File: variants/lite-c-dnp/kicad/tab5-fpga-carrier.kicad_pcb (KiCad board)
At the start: 4 copper layers, 125 x 78 mm, 116 parts, among them J1 DC 12V ONLY, J2 USB-C PD in, J3 M5-BUS (to Tab5), J4 SOCKET XDAP-4042044-20401, J5 HDMI OUT, J6 PMOD1, J7 PMOD2, J8 GPIO pads, Q1 2N7002, Q2 2N7002, Q3 2N7002, Q4 2N7002, SW1 SW, SW2 RESET (Tab5), SW3 FPGA ON/OFF, U1 CH224K, U10 TPS3839K50DBZR, U2 TPS5430DDAR, U3 XC6206P332MR-G, U4 RCLAMP0524P, U5 RCLAMP0524P, U6 SRV05-4, U7 SN74CB3Q3245PWR, U8 SN74CB3Q3245PWR, U9 TPS3839G33DBZR

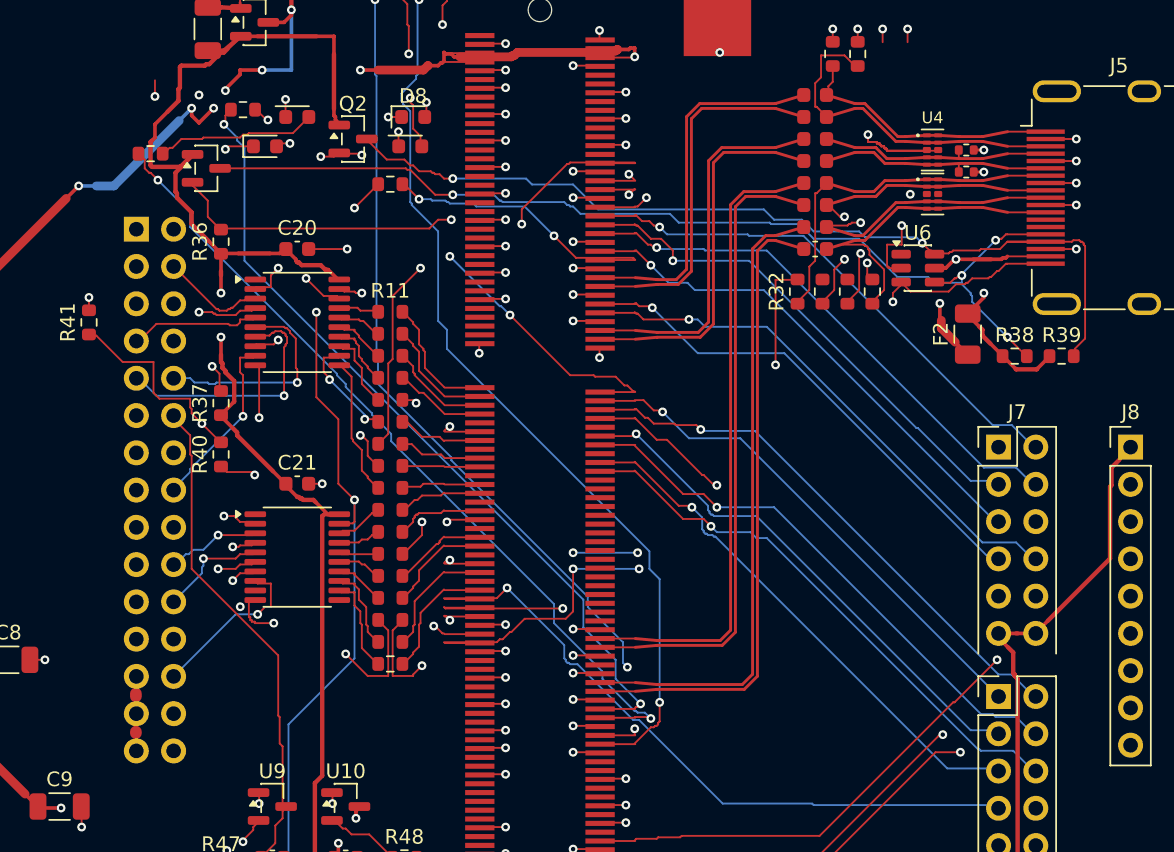
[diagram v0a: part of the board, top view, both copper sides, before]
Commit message: Qualify lite variants for conditional PoC fabrication and publish per-board reports
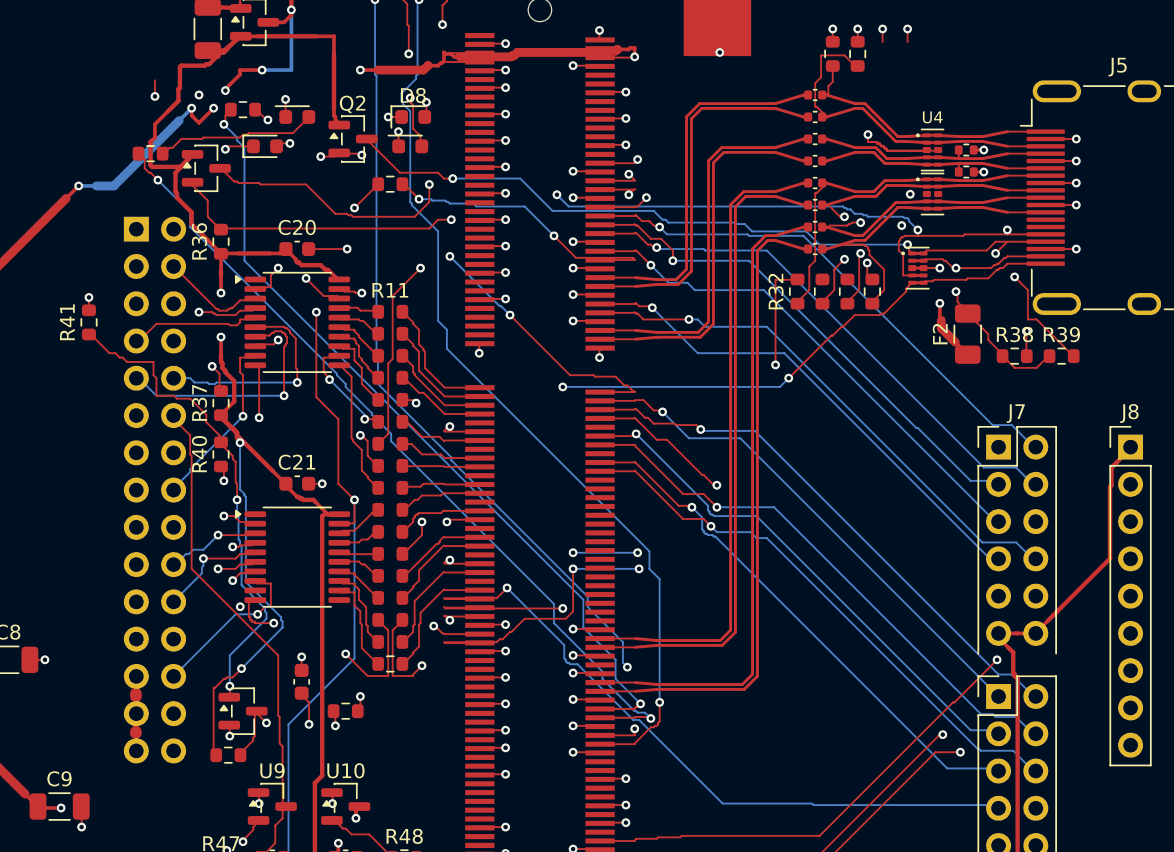
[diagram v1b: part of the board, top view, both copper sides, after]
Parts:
- added C24: 100n, C_0603_1608Metric, F.Cu at (65.0, 53.0)
- added Q5: MMBT3904, SOT-23, F.Cu at (61.0, 55.0)
- added R51: 47k, R_0603_1608Metric, F.Cu at (60.0, 58.0)
- added R52: 10k, R_0603_1608Metric, F.Cu at (68.0, 55.0)
- C12, C13, C14, C15, C16, C17, C18, C19: footprint C_0603_1608Metric -> C_0402_1005Metric
- R10, R11, R12, R13, R14, R15, R16, R19, R20, R21, R22, R23, R24, R26, R27: value 33R -> 680R
- R40: value 10k -> 47k
- R41: value 20k -> 100k
- U6: value SRV05-4 -> RCLAMP0524P; footprint SOT-23-6 -> DFN2510-10L_RCLAMP0524P
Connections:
- R40 pad 2: F_HPD -> HPD_B
- R41 pad 1: F_HPD -> HPD_B
- U6 pad 1: (no net) -> HDMI_SDA
- U6 pad 2: GND -> HDMI_5V
- U6 pad 3: HDMI_HPD -> GND
- U6 pad 5: HDMI_5V -> HDMI_HPD
- U6 pad 6: HDMI_SDA -> HDMI_HPD
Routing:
- net HPD_B: track 0.00 -> 33.4 mm, vias 0 -> 2
- net +3V3: track 189.1 -> 216.4 mm, vias 3 -> 5
- net HPD_BUF: track 0.00 -> 12.7 mm, vias 0 -> 3
- net HDMI_SCL: track 70.2 -> 76.8 mm, vias 4 -> 5
- net F_HPD: track 54.0 -> 48.2 mm
- net HDMI_SDA: track 63.3 -> 61.5 mm, vias 2 -> 4
- net HDMI_5V: track 20.9 -> 21.7 mm
- net HDMI_HPD: track 63.3 -> 64.1 mm, vias 2 -> 3
- net GND: track 187.6 -> 188.1 mm, vias 109 -> 112

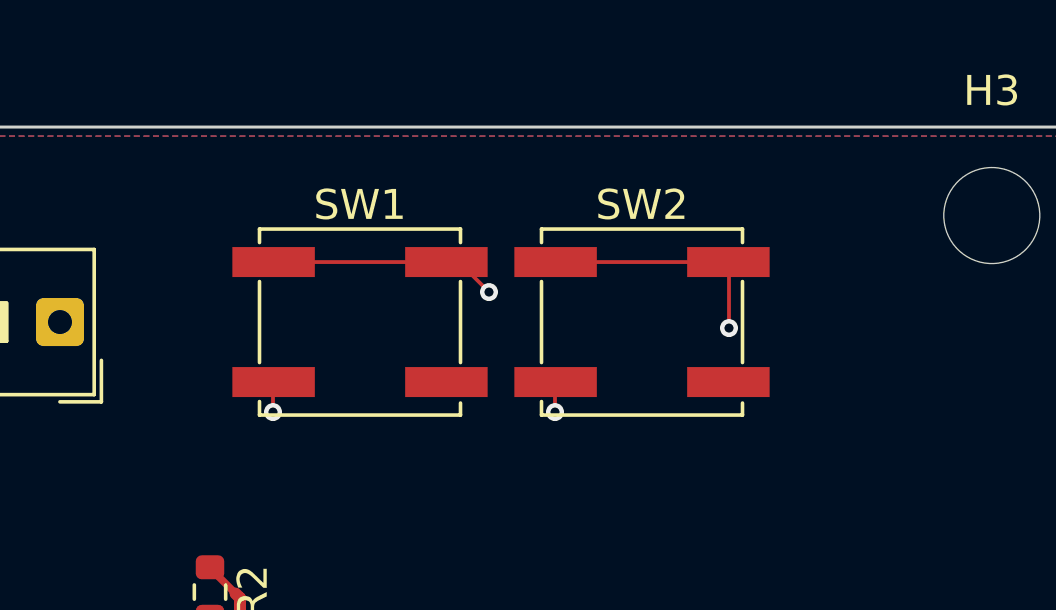
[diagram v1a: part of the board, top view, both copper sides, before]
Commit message: Align variants B and C with Akizuki buttons and explain A BOM
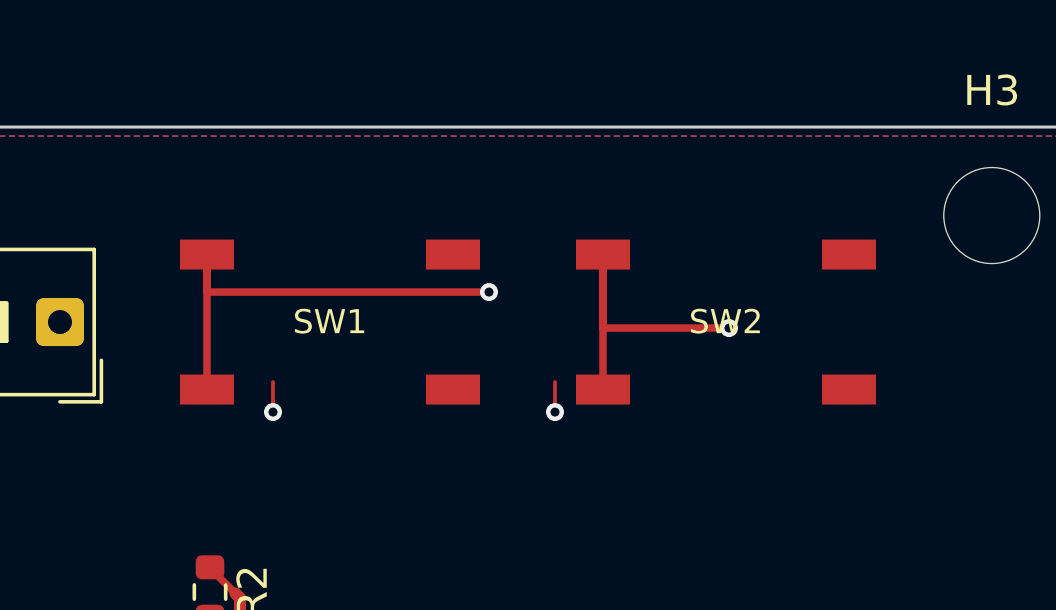
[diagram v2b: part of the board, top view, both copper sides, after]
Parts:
- SW1: value SW -> TS-06104; footprint SW_SPST_EVQP0 -> carrier:SW_TS_06104_HandSolder
- SW2: value RESET (Tab5) -> TS-06104; footprint SW_SPST_EVQP0 -> carrier:SW_TS_06104_HandSolder
- moved SW2 2.80 mm to (42.2, 7.50)
- moved SW1 1.00 mm to (29.0, 7.50)
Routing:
- net F_BTN0: track 74.5 -> 82.0 mm
- net TAB_RST: track 33.3 -> 36.4 mm
